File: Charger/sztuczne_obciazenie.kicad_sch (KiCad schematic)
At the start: 26 parts, among them Q13 BC846BW, Q14 MJD31CT4, Q15 BUJ302AD, Q16 BUJ302AD, U11 MCP6001-OT, U7 MCP6001-OT, U8 MCP6001-OT, U9 MCP6001-OT

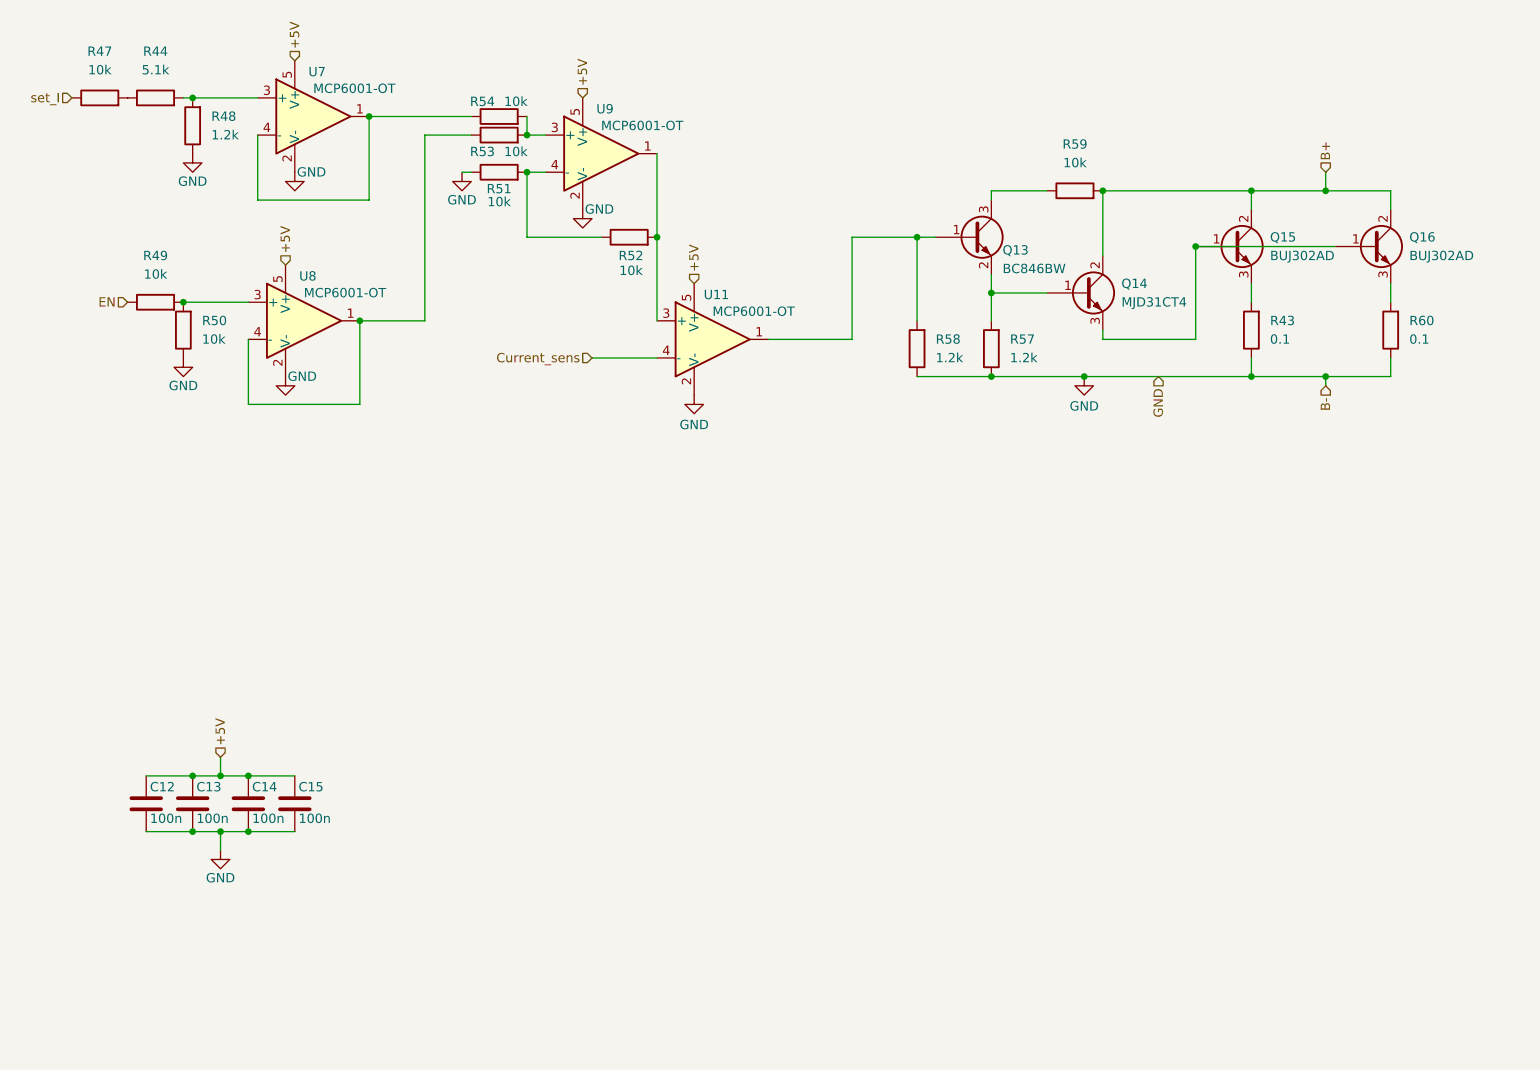
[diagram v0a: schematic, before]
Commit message: dodana ladowarka do glownego projektu
drobne zmiany w sumie wszedzie pozbyłem sie 3.3v poza sterowaniem z pinów mcu, dopiescilem rezystorki zby bylo jak najmniej wartości rozszerzylem delikatnie zakres pradowy przetwornicy
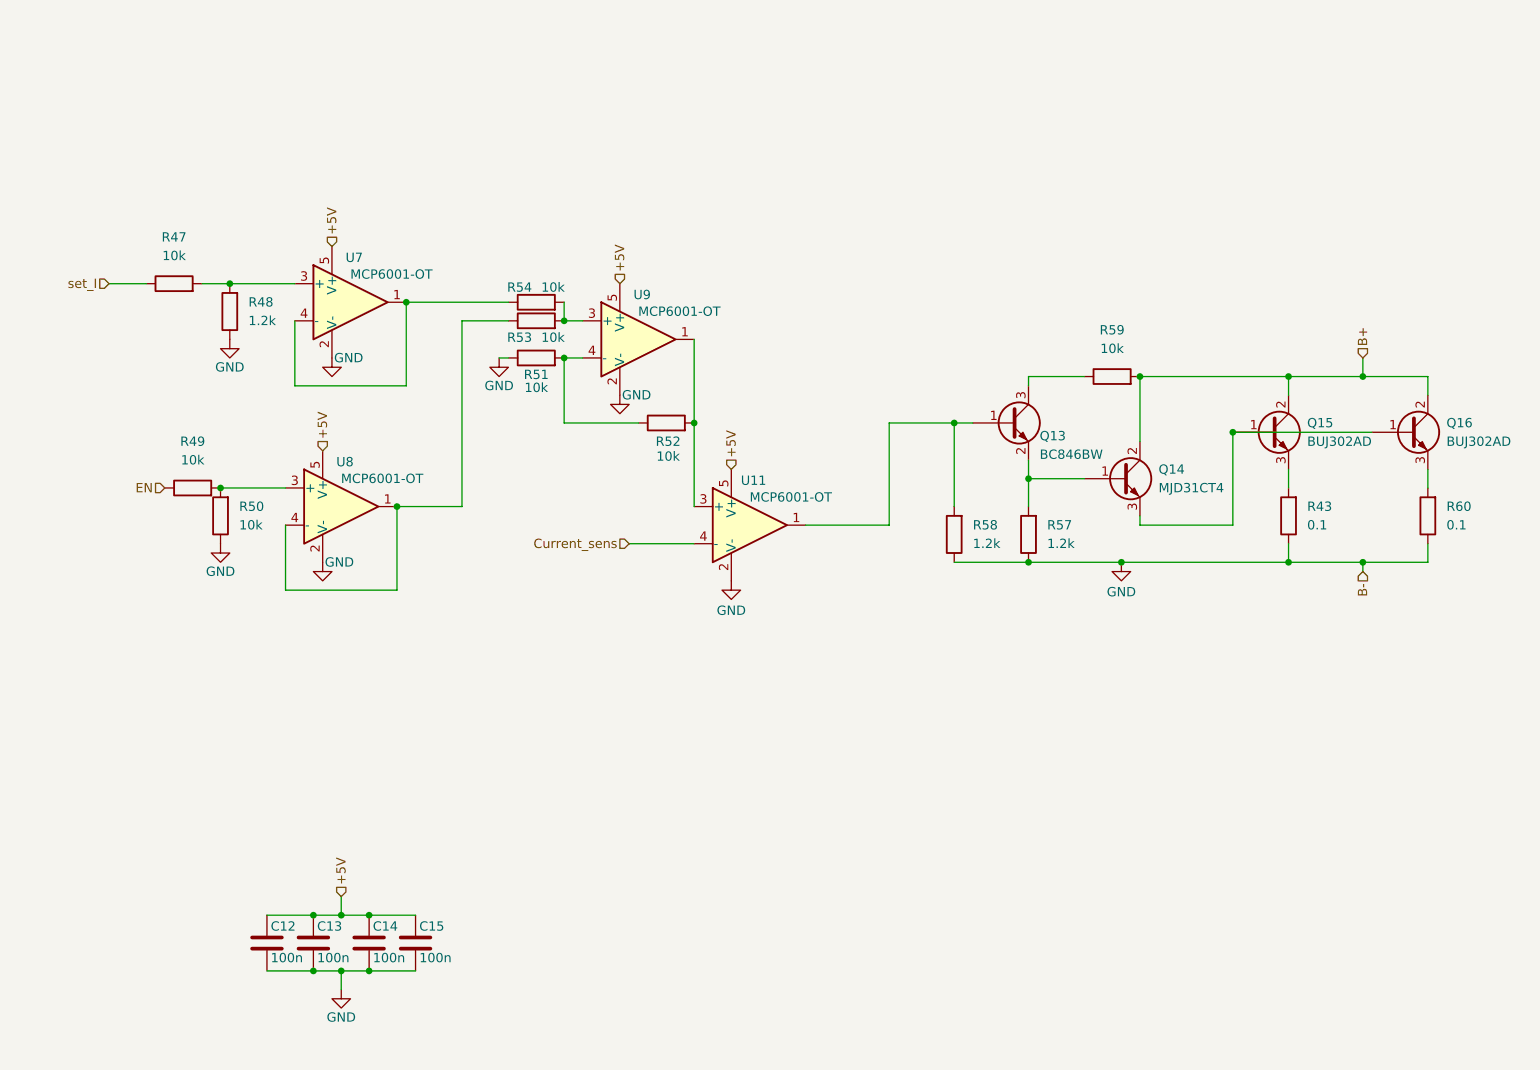
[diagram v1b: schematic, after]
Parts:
- removed R44: 5.1k, Resistor_SMD:R_0805_2012Metric_Pad1.20x1.40mm_HandSolder, symbol Device:R
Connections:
- net at R48.2, U7.3 (+): now also R47.2
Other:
- moved on the sheet: C12, C13, C14, C15, Q13, Q14, Q15, Q16, R43, R47, R48, R49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

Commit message: pcb up
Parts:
- removed C12, C13, C14: 100n, Capacitor_SMD:C_0805_2012Metric_Pad1.18x1.45mm_HandSolder, symbol Device:C
- removed U11, U7, U8, U9: MCP6001-OT, Package_TO_SOT_SMD:SOT-23-5, symbol Amplifier_Operational:MCP6001-OT
- added U13: MCP6004, Package_SO:SOIC-14_3.9x8.7mm_P1.27mm, symbol Amplifier_Operational:MCP6004
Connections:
- net +5V: now also U13.4 (V+)
- net Current_sens: now also U13.13 (-)
- net GND: now also U13.11 (V-)
- net at R49.2, R50.2: now also U13.10 (+)
- net at R47.2, R48.2: now also U13.3 (+)
- net at R54.1: now also U13.1, U13.2 (-)
- net at R51.2, R52.1: now also U13.6 (-)
- net at Q13.1 (B), R58.2: now also U13.14
- net at R52.2: now also U13.12 (+), U13.7
- net at R53.2, R54.2: now also U13.5 (+)
- net at R53.1: now also U13.8, U13.9 (-)
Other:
- moved on the sheet: C15

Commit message: small update
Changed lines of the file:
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@@
-	(symbol
-		(lib_id "power:GND")
-		(at 139.7 113.03 0)
-		(unit 1)
-		(exclude_from_sim no)
-		(in_bom yes)
-		(on_board yes)
-		(dnp no)
-		(property "Reference" "#PWR035"
-			(at 139.7 119.38 0)
-			(effects
-				(font
-					(size 1.27 1.27)
-				)
-				(hide yes)
-			)
-		)
-		(property "Value" "GND"
-			(at 139.7 117.094 0)
-			(effects
-				(font
-					(size 1.27 1.27)
-				)
-				(hide yes)
-			)
-		)
-		(property "Footprint" ""
-			(at 139.7 113.03 0)
-			(effects
-				(font
-					(size 1.27 1.27)
-				)
-				(hide yes)
-			)
-		)
-		(property "Datasheet" ""
-			(at 139.7 113.03 0)
-			(effects
-				(font
-					(size 1.27 1.27)
-				)
-				(hide yes)
-			)
-		)
-		(property "Description" "Power symbol creates a global label with name \"GND\" , ground"
-			(at 139.7 113.03 0)
-			(effects
-				(font
-					(size 1.27 1.27)
-				)
-				(hide yes)
-			)
-		)
-		(pin "1"
-		)
-		(instances
-			(project "Charger"
-				(path "/f0501846-9b00-4ec1-8596-952177c35a04/4a43665d-51a2-43d4-ad69-04fcbc176fe7"
-					(reference "#PWR035")
-					(unit 1)
-				)
-			)
-		)
-	)
 	(symbol
 		(lib_id "power:GND")

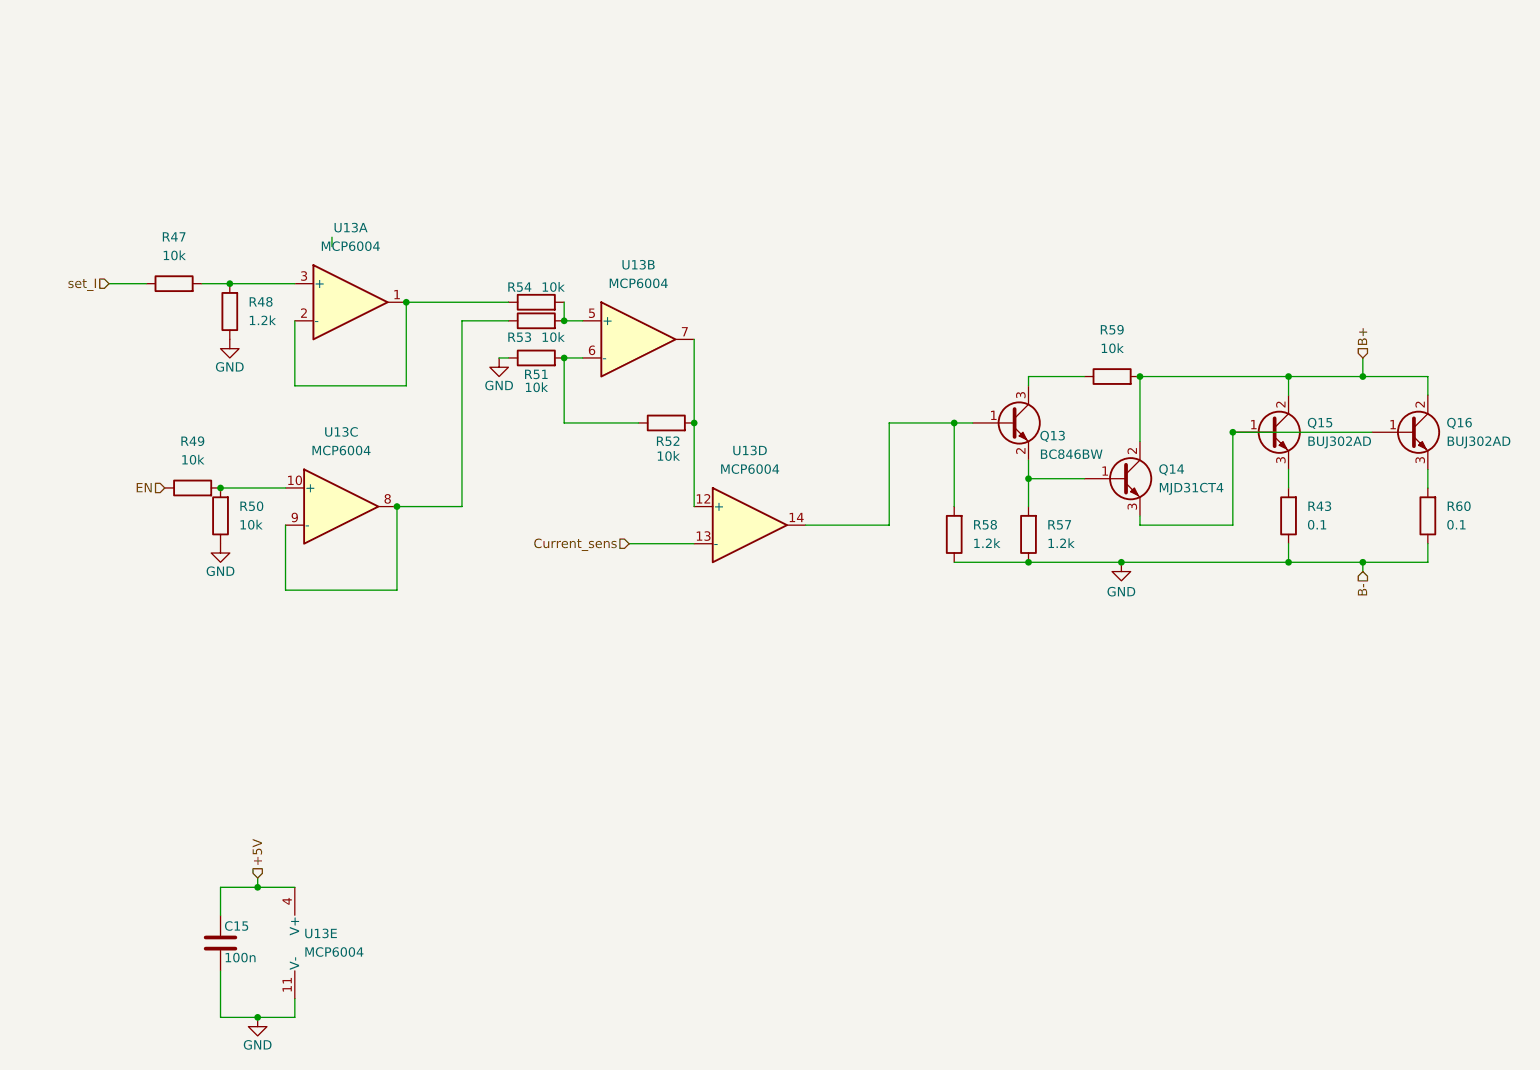
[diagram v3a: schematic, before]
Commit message: aktualizacja schematu
nie zmieniałem nic na pcb
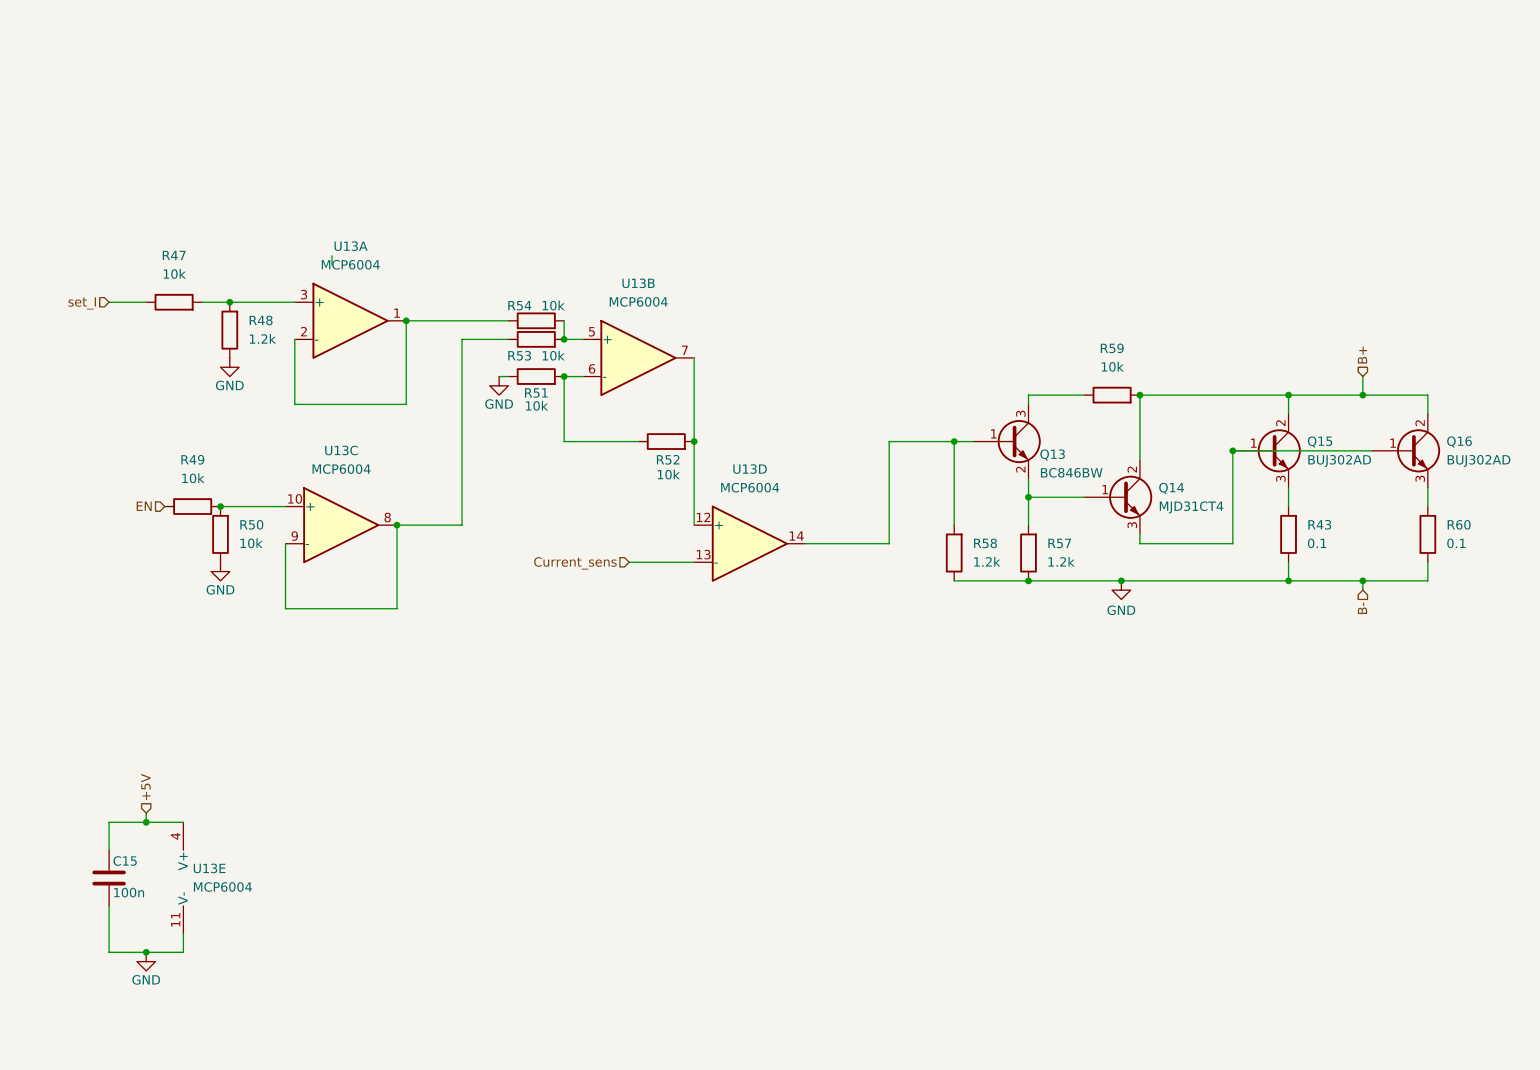
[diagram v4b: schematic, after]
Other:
- moved on the sheet: C15, Q13, Q14, Q15, Q16, R43, R47, R48, R49, R50, R51, R52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
